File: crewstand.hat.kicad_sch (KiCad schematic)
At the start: 18 parts, among them J1 GPIO, J2 CAN Terminal, J3 Sensor Terminal, J4 V-In, J6 V-Out, J7 Relais2, J8 Relais1, U2 MCP2515-xSO, U3 MCP2551-I-P, U4 PicoW, Y2 12M

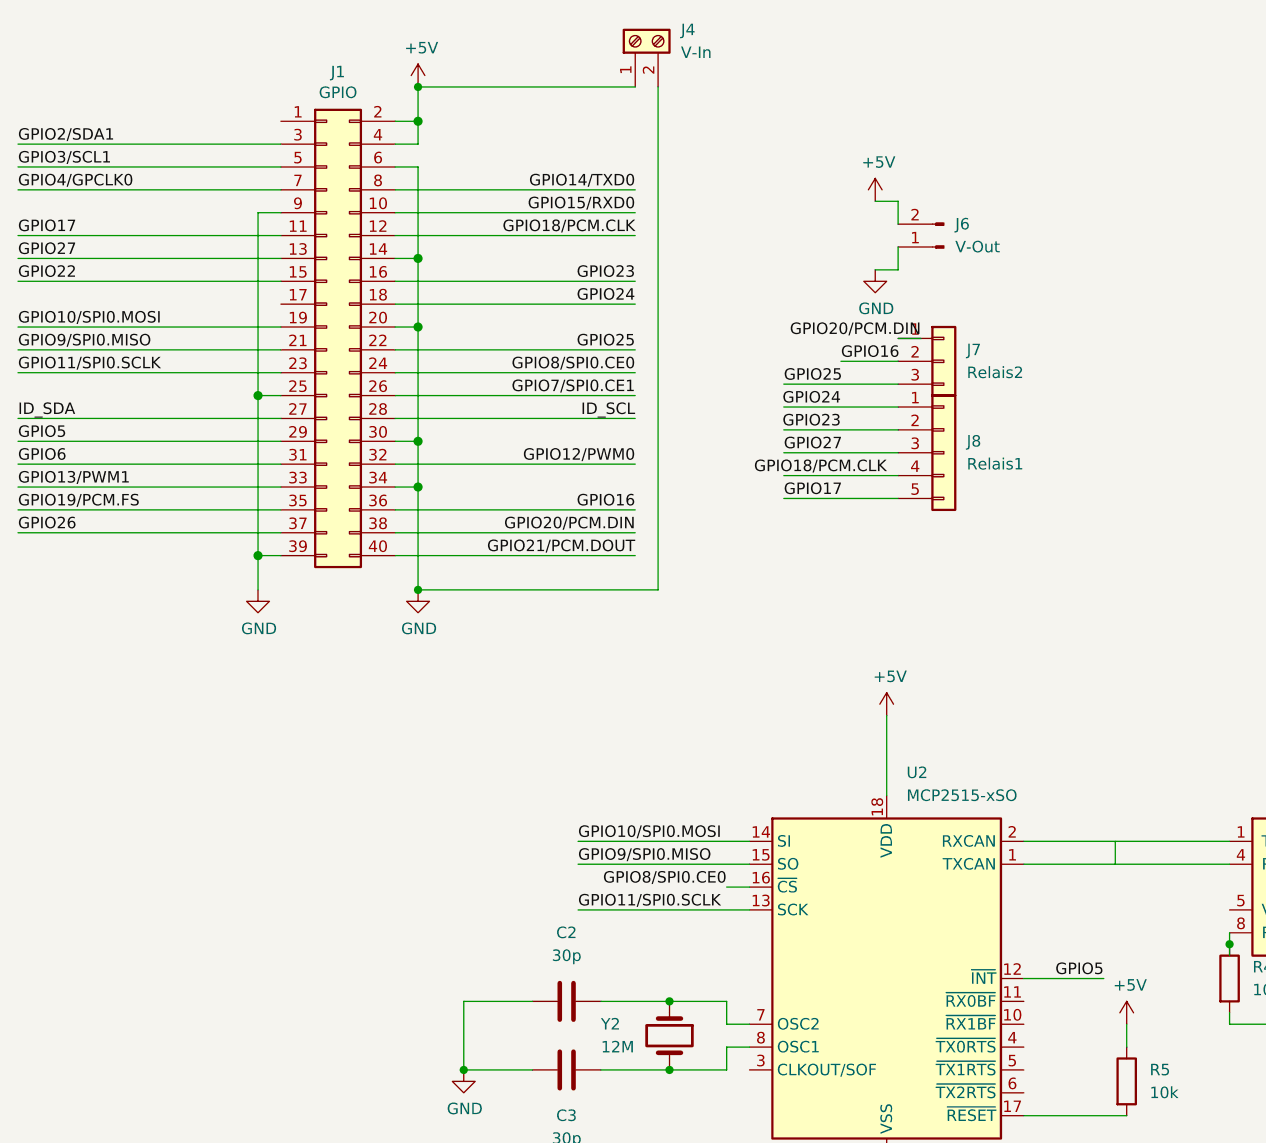
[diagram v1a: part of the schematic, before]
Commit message: feat!: reorder for bottom placement
* Bottom placement needed to have connectors accessible on top
* optimize trace width
* optimise for voroni design
* include [pcb2gcode](https://github.com/pcb2gcode/pcb2gcode) generated svg for cnc

BREAKING CHANGE: Platine Layout for bottom
  placement of the Parts
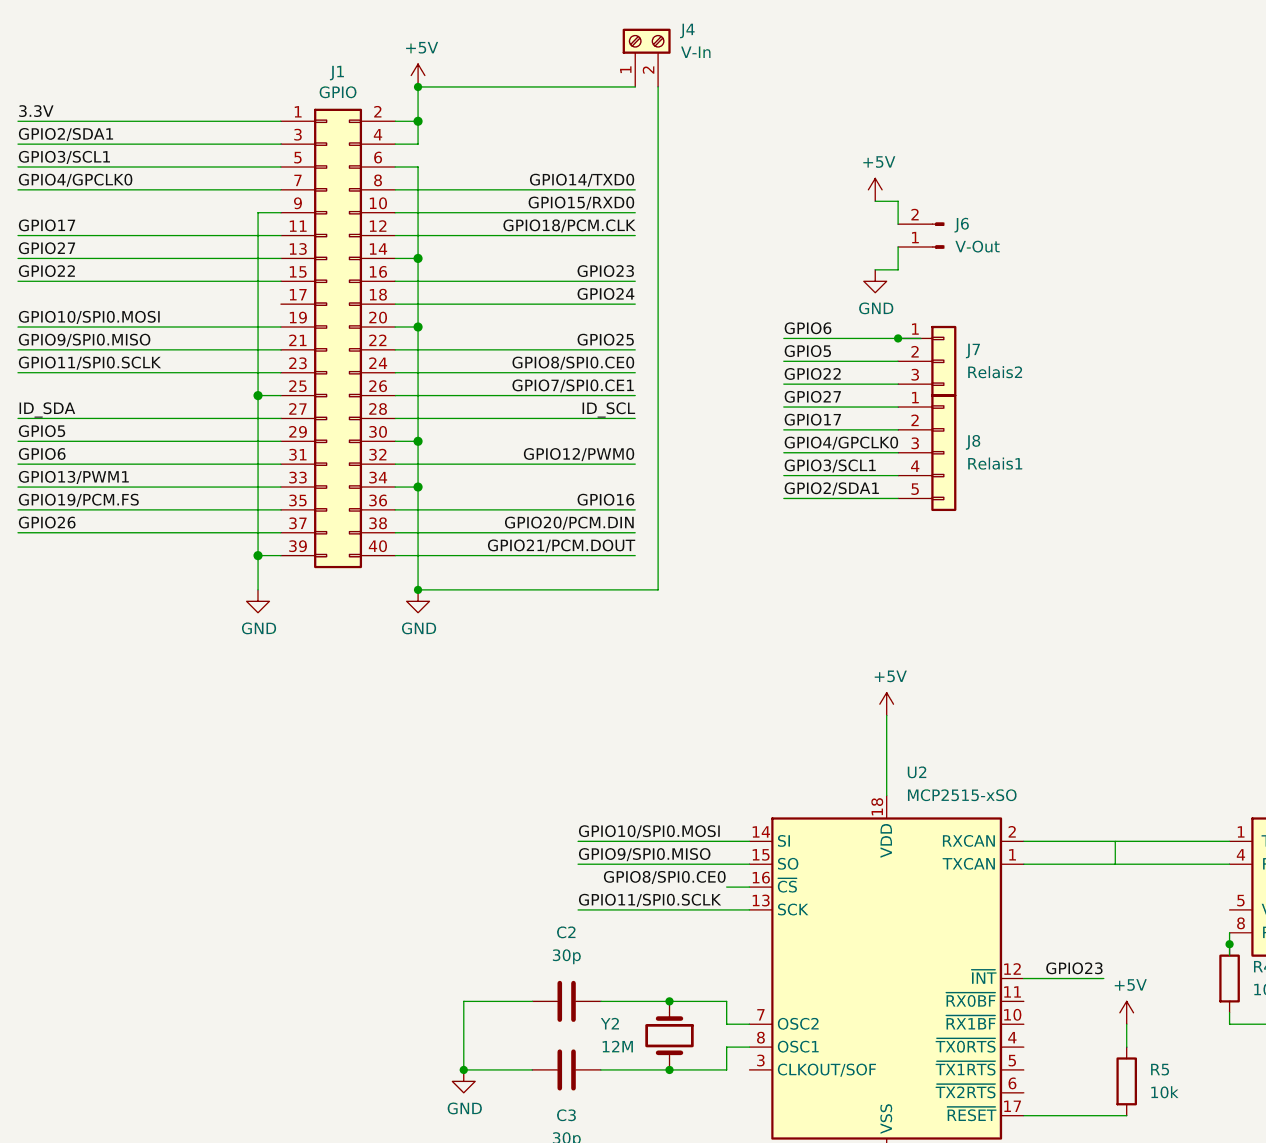
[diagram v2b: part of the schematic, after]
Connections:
- net GPIO16: no longer J7.2 (Pin_2)
- net GPIO17: now also J8.2 (Pin_2); no longer J8.5 (Pin_5)
- net GPIO18/PCM.CLK: no longer J8.4 (Pin_4)
- net GPIO20/PCM.DIN: no longer J7.1 (Pin_1)
- net GPIO22: now also J7.3 (Pin_3)
- net GPIO23: now also U2.12 (~{INT}); no longer J8.2 (Pin_2)
- net GPIO24: no longer J8.1 (Pin_1)
- net GPIO25: no longer J7.3 (Pin_3)
- net GPIO27: now also J8.1 (Pin_1); no longer J8.3 (Pin_3)
- net GPIO2/SDA1: now also J8.5 (Pin_5)
- net GPIO3/SCL1: now also J8.4 (Pin_4)
- net GPIO4/GPCLK0: now also J8.3 (Pin_3)
- net GPIO5: now also J7.2 (Pin_2); no longer U2.12 (~{INT})
- net GPIO6: now also J7.1 (Pin_1)
- net 3.3V: now reaches J1.1 (Pin_1)
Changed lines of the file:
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@@
   (junction (at 166.37 119.38) (diameter 0) (color 0 0 0 0)
+  )
+  (junction (at 129.54 52.07) (diameter 0) (color 0 0 0 0)
   )
   (junction (at 241.3 59.69) (diameter 0) (color 0 0 0 0)
@@
     (stroke (width 0) (type default))
   )
+  (wire (pts (xy 31.75 27.94) (xy 60.96 27.94))
+    (stroke (width 0) (type default))
+  )
   (wire (pts (xy 76.2 50.8) (xy 76.2 63.5))
     (stroke (width 0) (type solid))
@@
     (stroke (width 0) (type solid))
   )
+  (wire (pts (xy 116.84 52.07) (xy 129.54 52.07))
+    (stroke (width 0) (type default))
+  )
   (wire (pts (xy 143.51 107.95) (xy 166.37 107.95))
     (stroke (width 0) (type default))
@@
     (stroke (width 0) (type default))
   )
-  (wire (pts (xy 123.19 54.61) (xy 129.54 54.61))
+  (wire (pts (xy 116.84 54.61) (xy 129.54 54.61))
     (stroke (width 0) (type default))
   )
@@
     (effects (font (size 1.27 1.27)) (justify left bottom))
   )
+  (label "GPIO4{slash}GPCLK0" (at 116.84 64.77 0) (fields_autoplaced)
+    (effects (font (size 1.27 1.27)) (justify left bottom))
+  )
+  (label "GPIO3{slash}SCL1" (at 116.84 67.31 0) (fields_autoplaced)
+    (effects (font (size 1.27 1.27)) (justify left bottom))
+  )
+  (label "GPIO27" (at 116.84 59.69 0) (fields_autoplaced)
+    (effects (font (size 1.27 1.27)) (justify left bottom))
+  )
   (label "VSYS" (at 255.27 31.75 180) (fields_autoplaced)
     (effects (font (size 1.27 1.27)) (justify right bottom))
   )
+  (label "GPIO17" (at 116.84 62.23 0) (fields_autoplaced)
+    (effects (font (size 1.27 1.27)) (justify left bottom))
+  )
   (label "ID_SDA" (at 31.75 60.96 0) (fields_autoplaced)
     (effects (font (size 1.27 1.27)) (justify left bottom))
   )
   (label "GPIO6" (at 31.75 66.04 0) (fields_autoplaced)
-    (effects (font (size 1.27 1.27)) (justify left bottom))
-  )
-  (label "GPIO17" (at 116.84 69.85 0) (fields_autoplaced)
     (effects (font (size 1.27 1.27)) (justify left bottom))
   )
@@
     (effects (font (size 1.27 1.27)) (justify left bottom))
   )
+  (label "GPIO2{slash}SDA1" (at 116.84 69.85 0) (fields_autoplaced)
+    (effects (font (size 1.27 1.27)) (justify left bottom))
+  )
   (label "GPIO23" (at 100.33 45.72 180) (fields_autoplaced)
     (effects (font (size 1.27 1.27)) (justify right bottom))
@@
     (effects (font (size 1.27 1.27)) (justify right bottom))
   )
-  (label "GPIO25" (at 116.84 57.15 0) (fields_autoplaced)
-    (effects (font (size 1.27 1.27)) (justify left bottom))
-  )
-  (label "GPIO24" (at 123.19 59.69 180) (fields_autoplaced)
-    (effects (font (size 1.27 1.27)) (justify right bottom))
-  )
   (label "GPIO16" (at 100.33 71.12 180) (fields_autoplaced)
     (effects (font (size 1.27 1.27)) (justify right bottom))
@@
     (effects (font (size 1.27 1.27)) (justify left bottom))
   )
-  (label "GPIO18{slash}PCM.CLK" (at 128.27 67.31 180) (fields_autoplaced)
-    (effects (font (size 1.27 1.27)) (justify right bottom))
-  )
   (label "GPIO14{slash}TXD0" (at 257.81 74.93 180) (fields_autoplaced)
     (effects (font (size 1.27 1.27)) (justify right bottom))
@@
     (effects (font (size 1.27 1.27)) (justify left bottom))
   )
-  (label "GPIO20{slash}PCM.DIN" (at 132.08 52.07 180) (fields_autoplaced)
-    (effects (font (size 1.27 1.27)) (justify right bottom))
-  )
   (label "GPIO17" (at 31.75 40.64 0) (fields_autoplaced)
     (effects (font (size 1.27 1.27)) (justify left bottom))
   )
-  (label "GPIO16" (at 123.19 54.61 0) (fields_autoplaced)
+  (label "GPIO6" (at 116.84 52.07 0) (fields_autoplaced)
     (effects (font (size 1.27 1.27)) (justify left bottom))
   )
@@
     (effects (font (size 1.27 1.27)) (justify right bottom))
   )
-  (label "GPIO23" (at 123.19 62.23 180) (fields_autoplaced)
-    (effects (font (size 1.27 1.27)) (justify right bottom))
-  )
   (label "GPIO3{slash}SCL1" (at 31.75 33.02 0) (fields_autoplaced)
     (effects (font (size 1.27 1.27)) (justify left bottom))
@@
     (effects (font (size 1.27 1.27)) (justify right bottom))
   )
+  (label "GPIO5" (at 116.84 54.61 0) (fields_autoplaced)
+    (effects (font (size 1.27 1.27)) (justify left bottom))
+  )
   (label "GPIO8{slash}SPI0.CE0" (at 110.49 113.03 180) (fields_autoplaced)
     (effects (font (size 1.27 1.27)) (justify right bottom))
   )
+  (label "GPIO22" (at 116.84 57.15 0) (fields_autoplaced)
+    (effects (font (size 1.27 1.27)) (justify left bottom))
+  )
+  (label "3.3V" (at 31.75 27.94 0) (fields_autoplaced)
+    (effects (font (size 1.27 1.27)) (justify left bottom))
+  )
   (label "GPIO15{slash}RXD0" (at 257.81 77.47 180) (fields_autoplaced)
     (effects (font (size 1.27 1.27)) (justify right bottom))
@@
     (effects (font (size 1.27 1.27)) (justify left bottom))
   )
-  (label "GPIO27" (at 116.84 64.77 0) (fields_autoplaced)
-    (effects (font (size 1.27 1.27)) (justify left bottom))
-  )
-  (label "GPIO5" (at 152.4 123.19 180) (fields_autoplaced)
+  (label "GPIO23" (at 152.4 123.19 180) (fields_autoplaced)
     (effects (font (size 1.27 1.27)) (justify right bottom))
   )
